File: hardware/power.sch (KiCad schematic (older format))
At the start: 18 parts, among them SW1 PM_BTN, U2 TPS63031DSKR, U5 BQ24075RGTT, U6 MAX16054AZT+T

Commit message: Removed 72 LEDs
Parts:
- BT1: symbol Battery -> Battery-RESCUE-blupoi
- L2: footprint Capacitors_SMD:C_0603 -> Resistors_SMD:R_1206
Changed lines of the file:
@@
 LIBS:micro_b_usb
 LIBS:blupoi-cache
-EELAYER 25 0
+EELAYER 26 0
 EELAYER END
 $Descr A4 11693 8268
@@
 F 0 "L2" H 4950 1865 50  0000 C CNN
 F 1 "1.5uH" H 4950 1774 50  0000 C CNN
-F 2 "Capacitors_SMD:C_0603" H 4950 1650 50  0001 C CNN
+F 2 "Resistors_SMD:R_1206" H 4950 1650 50  0001 C CNN
 F 3 "" H 4950 1650 50  0000 C CNN
 	1    4950 1650
@@
 $EndComp
 $Comp
-L Battery BT1
+L Battery-RESCUE-blupoi BT1
 U 1 1 579AD18C
 P 1850 2150
+AR Path="/579AD18C" Ref="BT1"  Part="1"
+AR Path="/57B9A02C/579AD18C" Ref="BT1"  Part="1"
 F 0 "BT1" V 1595 2150 50  0000 C CNN
 F 1 "Battery" V 1686 2150 50  0000 C CNN

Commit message: Power, add pulldown to bq24075 EN1
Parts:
- added R?: 10k, symbol R_Small
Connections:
- wire segments 81 -> 83
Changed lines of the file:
@@
 $Descr A4 11693 8268
 encoding utf-8
-Sheet 7 6
+Sheet 6 6
 Title ""
 Date ""
@@
 Text HLabel 6250 4750 2    60   Input ~ 0
 PM_EN2
-Text HLabel 5050 4850 2    60   Input ~ 0
+Text HLabel 6250 4850 2    60   Input ~ 0
 PM_EN1
 Text HLabel 5050 5050 2    60   Output ~ 0
@@
 	6050 4650 6050 4750
 Wire Wire Line
-	5050 4850 4950 4850
+	4950 4850 6250 4850
 Wire Wire Line
 	5250 5350 4950 5350
@@
 Text GLabel 3650 6850 0    60   Input ~ 0
 VBAT
+$Comp
+L R_Small R?
+U 1 1 5897F73B
+P 6050 5050
+F 0 "R?" H 6100 5150 50  0000 L CNN
+F 1 "10k" H 6100 4950 50  0000 L CNN
+F 2 "" H -100 100 50  0001 C CNN
+F 3 "" H -100 100 50  0001 C CNN
+	1    6050 5050
+	1    0    0    -1
+$EndComp
+Wire Wire Line
+	6050 4950 6050 4850
+Connection ~ 6050 4850
+$Comp
+L GND #PWR?
+U 1 1 5897F92D
+P 6050 5300
+F 0 "#PWR?" H 6100 5350 50  0001 C CNN
+F 1 "GND" H 6055 5127 50  0000 C CNN
+F 2 "" H -50 0   50  0001 C CNN
+F 3 "" H -50 0   50  0001 C CNN
+	1    6050 5300
+	1    0    0    -1
+$EndComp
+Wire Wire Line
+	6050 5300 6050 5150
 $EndSCHEMATC

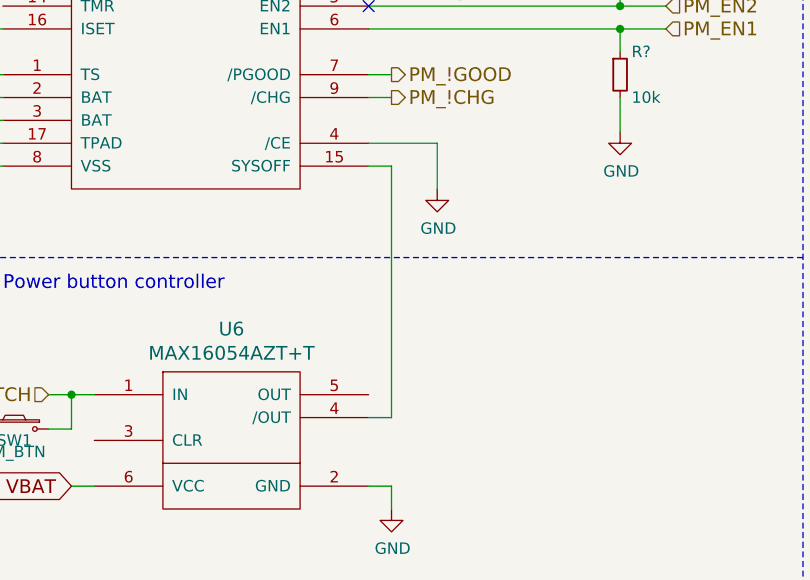
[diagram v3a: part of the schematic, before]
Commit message: Power, add pulldown to bq24075 SYSOFF
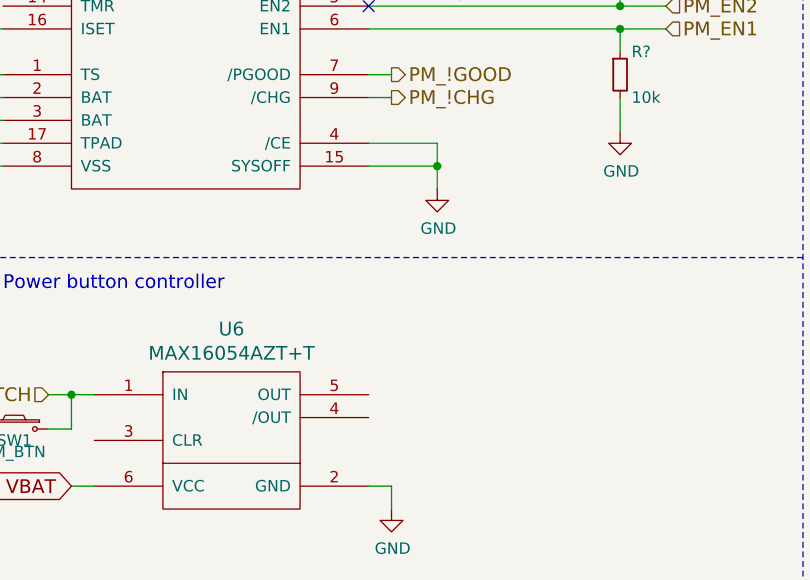
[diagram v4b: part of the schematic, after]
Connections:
- wire segments 83 -> 81
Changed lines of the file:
@@
 	3150 6600 3250 6600
 Wire Wire Line
-	4950 5450 5050 5450
-Wire Wire Line
-	5050 5450 5050 6550
-Wire Wire Line
-	5050 6550 4950 6550
+	4950 5450 5250 5450
 Wire Wire Line
 	3250 4450 3250 4300
@@
 Wire Wire Line
 	6050 5300 6050 5150
+Connection ~ 5250 5450
 $EndSCHEMATC

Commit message: Added sip32408 ic
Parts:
- added U7: sip32408, symbol sip32408
- R7: renamed from R?; footprint (none) -> Resistors_SMD:R_0603
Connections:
- net labels added: VCHG
- wire segments 81 -> 87
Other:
- moved on the sheet: SW1, U6
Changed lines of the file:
@@
 LIBS:max16054
 LIBS:micro_b_usb
+LIBS:sip32408
 LIBS:blupoi-cache
 EELAYER 26 0
@@
 $EndComp
 $Comp
-L GND #PWR017
+L GND #PWR23
 U 1 1 5794CAF3
 P 4200 2650
-F 0 "#PWR017" H 4200 2400 50  0001 C CNN
+F 0 "#PWR23" H 4200 2400 50  0001 C CNN
 F 1 "GND" H 4205 2477 50  0000 C CNN
 F 2 "" H 4200 2650 50  0000 C CNN
@@
 $EndComp
 $Comp
-L GND #PWR018
+L GND #PWR26
 U 1 1 5794CB19
 P 5750 2650
-F 0 "#PWR018" H 5750 2400 50  0001 C CNN
+F 0 "#PWR26" H 5750 2400 50  0001 C CNN
 F 1 "GND" H 5755 2477 50  0000 C CNN
 F 2 "" H 5750 2650 50  0000 C CNN
@@
 $EndComp
 $Comp
-L GND #PWR019
+L GND #PWR27
 U 1 1 5794D124
 P 5900 2550
-F 0 "#PWR019" H 5900 2300 50  0001 C CNN
+F 0 "#PWR27" H 5900 2300 50  0001 C CNN
 F 1 "GND" H 5905 2377 50  0000 C CNN
 F 2 "" H 5900 2550 50  0000 C CNN
@@
 $EndComp
 $Comp
-L GND #PWR020
+L GND #PWR29
 U 1 1 5794D140
 P 6200 2550
-F 0 "#PWR020" H 6200 2300 50  0001 C CNN
+F 0 "#PWR29" H 6200 2300 50  0001 C CNN
 F 1 "GND" H 6205 2377 50  0000 C CNN
 F 2 "" H 6200 2550 50  0000 C CNN
@@
 $EndComp
 $Comp
-L GND #PWR021
+L GND #PWR21
 U 1 1 5794D3C8
 P 3650 2550
-F 0 "#PWR021" H 3650 2300 50  0001 C CNN
+F 0 "#PWR21" H 3650 2300 50  0001 C CNN
 F 1 "GND" H 3655 2377 50  0000 C CNN
 F 2 "" H 3650 2550 50  0000 C CNN
@@
 $EndComp
 $Comp
-L GND #PWR022
+L GND #PWR17
 U 1 1 579AD335
 P 1600 2250
-F 0 "#PWR022" H 1600 2000 50  0001 C CNN
+F 0 "#PWR17" H 1600 2000 50  0001 C CNN
 F 1 "GND" H 1605 2077 50  0000 C CNN
 F 2 "" H 1600 2250 50  0000 C CNN
@@
 VUSB
 $Comp
-L GND #PWR023
+L GND #PWR20
 U 1 1 57B8A1CB
 P 3250 5550
-F 0 "#PWR023" H 3250 5300 50  0001 C CNN
+F 0 "#PWR20" H 3250 5300 50  0001 C CNN
 F 1 "GND" H 3255 5377 50  0000 C CNN
 F 2 "" H 3250 5550 50  0000 C CNN
@@
 PM_!CHG
 $Comp
-L GND #PWR024
+L GND #PWR24
 U 1 1 57B8B68E
 P 5250 5550
-F 0 "#PWR024" H 5250 5300 50  0001 C CNN
+F 0 "#PWR24" H 5250 5300 50  0001 C CNN
 F 1 "GND" H 5255 5377 50  0000 C CNN
 F 2 "" H 5250 5550 50  0000 C CNN
@@
 	1    0    0    -1
 $EndComp
-Text HLabel 5650 4050 2    60   Output ~ 0
+Text HLabel 5300 6400 2    60   Output ~ 0
 VIN
 $Comp
 L MAX16054 U6
 U 1 1 57B90098
-P 4350 6650
-F 0 "U6" H 4350 7137 60  0000 C CNN
-F 1 "MAX16054AZT+T" H 4350 7031 60  0000 C CNN
-F 2 "tinkerforge-libraries:SOT23-6" H 4350 6650 60  0001 C CNN
-F 3 "" H 4350 6650 60  0001 C CNN
-	1    4350 6650
-	1    0    0    -1
-$EndComp
-$Comp
-L GND #PWR025
+P 3100 6750
+F 0 "U6" H 3100 7237 60  0000 C CNN
+F 1 "MAX16054AZT+T" H 3100 7131 60  0000 C CNN
+F 2 "tinkerforge-libraries:SOT23-6" H 3100 6750 60  0001 C CNN
+F 3 "" H 3100 6750 60  0001 C CNN
+	1    3100 6750
+	1    0    0    -1
+$EndComp
+$Comp
+L GND #PWR22
 U 1 1 57B90631
-P 5050 6950
-F 0 "#PWR025" H 5050 6700 50  0001 C CNN
-F 1 "GND" H 5055 6777 50  0000 C CNN
-F 2 "" H 5050 6950 50  0000 C CNN
-F 3 "" H 5050 6950 50  0000 C CNN
-	1    5050 6950
-	1    0    0    -1
-$EndComp
-Text HLabel 3550 6450 0    60   Input ~ 0
+P 3800 7050
+F 0 "#PWR22" H 3800 6800 50  0001 C CNN
+F 1 "GND" H 3805 6877 50  0000 C CNN
+F 2 "" H 3800 7050 50  0000 C CNN
+F 3 "" H 3800 7050 50  0000 C CNN
+	1    3800 7050
+	1    0    0    -1
+$EndComp
+Text HLabel 2300 6550 0    60   Input ~ 0
 PM_SWITCH
 $Comp
 L SW_PUSH_SMALL_H SW1
 U 1 1 57B90C56
-P 3400 6600
-F 0 "SW1" H 3400 6550 50  0000 C CNN
-F 1 "PM_BTN" H 3400 6500 50  0000 C CNN
-F 2 "footprints:switch_spst_smd_5.5mm_4.5mm" H 3400 6800 50  0001 C CNN
-F 3 "" H 3400 6800 50  0000 C CNN
-	1    3400 6600
-	1    0    0    -1
-$EndComp
-$Comp
-L GND #PWR026
+P 2150 6700
+F 0 "SW1" H 2150 6650 50  0000 C CNN
+F 1 "PM_BTN" H 2150 6600 50  0000 C CNN
+F 2 "footprints:switch_spst_smd_5.5mm_4.5mm" H 2150 6900 50  0001 C CNN
+F 3 "" H 2150 6900 50  0000 C CNN
+	1    2150 6700
+	1    0    0    -1
+$EndComp
+$Comp
+L GND #PWR18
 U 1 1 57B911A1
-P 3150 6700
-F 0 "#PWR026" H 3150 6450 50  0001 C CNN
-F 1 "GND" H 3155 6527 50  0000 C CNN
-F 2 "" H 3150 6700 50  0000 C CNN
-F 3 "" H 3150 6700 50  0000 C CNN
-	1    3150 6700
+P 1900 6800
+F 0 "#PWR18" H 1900 6550 50  0001 C CNN
+F 1 "GND" H 1905 6627 50  0000 C CNN
+F 2 "" H 1900 6800 50  0000 C CNN
+F 3 "" H 1900 6800 50  0000 C CNN
+	1    1900 6800
 	1    0    0    -1
 $EndComp
@@
 $EndComp
 $Comp
-L GND #PWR027
+L GND #PWR19
 U 1 1 57B91E3C
 P 2850 4450
-F 0 "#PWR027" H 2850 4200 50  0001 C CNN
+F 0 "#PWR19" H 2850 4200 50  0001 C CNN
 F 1 "GND" V 2855 4322 50  0000 R CNN
 F 2 "" H 2850 4450 50  0000 C CNN
@@
 Connection ~ 5050 4450
 Wire Wire Line
-	5050 6950 5050 6850
-Wire Wire Line
-	5050 6850 4950 6850
-Wire Wire Line
-	3750 6850 3650 6850
-Wire Wire Line
-	3550 6450 3750 6450
-Wire Wire Line
-	3650 6450 3650 6600
-Wire Wire Line
-	3650 6600 3550 6600
-Connection ~ 3650 6450
-Wire Wire Line
-	3150 6700 3150 6600
-Wire Wire Line
-	3150 6600 3250 6600
+	3800 7050 3800 6950
+Wire Wire Line
+	3800 6950 3700 6950
+Wire Wire Line
+	2500 6950 2400 6950
+Wire Wire Line
+	2300 6550 2500 6550
+Wire Wire Line
+	2400 6550 2400 6700
+Wire Wire Line
+	2400 6700 2300 6700
+Connection ~ 2400 6550
+Wire Wire Line
+	1900 6800 1900 6700
+Wire Wire Line
+	1900 6700 2000 6700
 Wire Wire Line
 	4950 5450 5250 5450
@@
 	5050 4050 5050 4550
 $Comp
-L GND #PWR028
+L GND #PWR25
 U 1 1 57BA2103
 P 5400 4550
-F 0 "#PWR028" H 5400 4300 50  0001 C CNN
+F 0 "#PWR25" H 5400 4300 50  0001 C CNN
 F 1 "GND" H 5400 4400 50  0000 C CNN
 F 2 "" H 5400 4550 50  0000 C CNN
@@
 Wire Wire Line
 	5400 4550 5400 4450
-Text GLabel 3650 6850 0    60   Input ~ 0
+Text GLabel 2400 6950 0    60   Input ~ 0
 VBAT
 $Comp
-L R_Small R?
+L R_Small R7
 U 1 1 5897F73B
 P 6050 5050
-F 0 "R?" H 6100 5150 50  0000 L CNN
+F 0 "R7" H 6100 5150 50  0000 L CNN
 F 1 "10k" H 6100 4950 50  0000 L CNN
-F 2 "" H -100 100 50  0001 C CNN
+F 2 "Resistors_SMD:R_0603" H -100 100 50  0001 C CNN
 F 3 "" H -100 100 50  0001 C CNN
 	1    6050 5050
@@
 Connection ~ 6050 4850
 $Comp
-L GND #PWR?
+L GND #PWR28
 U 1 1 5897F92D
 P 6050 5300
-F 0 "#PWR?" H 6100 5350 50  0001 C CNN
+F 0 "#PWR28" H 6100 5350 50  0001 C CNN
 F 1 "GND" H 6055 5127 50  0000 C CNN
 F 2 "" H -50 0   50  0001 C CNN
@@
 	6050 5300 6050 5150
 Connection ~ 5250 5450
+$Comp
+L sip32408 U7
+U 1 1 58980243
+P 4850 6300
+F 0 "U7" H 4875 6487 60  0000 C CNN
+F 1 "sip32408" H 4875 6381 60  0000 C CNN
+F 2 "" H -3550 1850 60  0001 C CNN
+F 3 "" H -3550 1850 60  0001 C CNN
+	1    4850 6300
+	1    0    0    -1
+$EndComp
+Wire Wire Line
+	4600 6400 4500 6400
+Wire Wire Line
+	4600 6550 3700 6550
+Wire Wire Line
+	5150 6550 5250 6550
+Wire Wire Line
+	5250 6550 5250 6700
+Wire Wire Line
+	5250 6700 5150 6700
+Wire Wire Line
+	5300 6400 5150 6400
+Text GLabel 5650 4050 2    60   Input ~ 0
+VCHG
+Text GLabel 4500 6400 0    60   Input ~ 0
+VCHG
 $EndSCHEMATC

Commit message: Switched to fat small design
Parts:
- removed BT1: Battery, 16650_holder:16650_in_pcb_socket, symbol Battery-RESCUE-blupoi
- added BT1: Battery_Cell, 16650_holder:16650_in_pcb_socket, symbol Battery_Cell
- U7: footprint (none) -> sip32408:sip32408
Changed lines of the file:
@@
 $EndComp
 $Comp
-L GND #PWR23
+L GND #PWR015
 U 1 1 5794CAF3
 P 4200 2650
-F 0 "#PWR23" H 4200 2400 50  0001 C CNN
+F 0 "#PWR015" H 4200 2400 50  0001 C CNN
 F 1 "GND" H 4205 2477 50  0000 C CNN
 F 2 "" H 4200 2650 50  0000 C CNN
@@
 $EndComp
 $Comp
-L GND #PWR26
+L GND #PWR016
 U 1 1 5794CB19
 P 5750 2650
-F 0 "#PWR26" H 5750 2400 50  0001 C CNN
+F 0 "#PWR016" H 5750 2400 50  0001 C CNN
 F 1 "GND" H 5755 2477 50  0000 C CNN
 F 2 "" H 5750 2650 50  0000 C CNN
@@
 $EndComp
 $Comp
-L GND #PWR27
+L GND #PWR017
 U 1 1 5794D124
 P 5900 2550
-F 0 "#PWR27" H 5900 2300 50  0001 C CNN
+F 0 "#PWR017" H 5900 2300 50  0001 C CNN
 F 1 "GND" H 5905 2377 50  0000 C CNN
 F 2 "" H 5900 2550 50  0000 C CNN
@@
 $EndComp
 $Comp
-L GND #PWR29
+L GND #PWR018
 U 1 1 5794D140
 P 6200 2550
-F 0 "#PWR29" H 6200 2300 50  0001 C CNN
+F 0 "#PWR018" H 6200 2300 50  0001 C CNN
 F 1 "GND" H 6205 2377 50  0000 C CNN
 F 2 "" H 6200 2550 50  0000 C CNN
@@
 $EndComp
 $Comp
-L GND #PWR21
+L GND #PWR019
 U 1 1 5794D3C8
 P 3650 2550
-F 0 "#PWR21" H 3650 2300 50  0001 C CNN
+F 0 "#PWR019" H 3650 2300 50  0001 C CNN
 F 1 "GND" H 3655 2377 50  0000 C CNN
 F 2 "" H 3650 2550 50  0000 C CNN
@@
 $EndComp
 $Comp
-L Battery-RESCUE-blupoi BT1
-U 1 1 579AD18C
-P 1850 2150
-AR Path="/579AD18C" Ref="BT1"  Part="1"
-AR Path="/57B9A02C/579AD18C" Ref="BT1"  Part="1"
-F 0 "BT1" V 1595 2150 50  0000 C CNN
-F 1 "Battery" V 1686 2150 50  0000 C CNN
-F 2 "16650_holder:16650_in_pcb_socket" V 1850 2190 50  0001 C CNN
-F 3 "" V 1850 2190 50  0000 C CNN
-	1    1850 2150
-	0    1    1    0
-$EndComp
-$Comp
-L GND #PWR17
+L GND #PWR020
 U 1 1 579AD335
 P 1600 2250
-F 0 "#PWR17" H 1600 2000 50  0001 C CNN
+F 0 "#PWR020" H 1600 2000 50  0001 C CNN
 F 1 "GND" H 1605 2077 50  0000 C CNN
 F 2 "" H 1600 2250 50  0000 C CNN
@@
 VUSB
 $Comp
-L GND #PWR20
+L GND #PWR021
 U 1 1 57B8A1CB
 P 3250 5550
-F 0 "#PWR20" H 3250 5300 50  0001 C CNN
+F 0 "#PWR021" H 3250 5300 50  0001 C CNN
 F 1 "GND" H 3255 5377 50  0000 C CNN
 F 2 "" H 3250 5550 50  0000 C CNN
@@
 PM_!CHG
 $Comp
-L GND #PWR24
+L GND #PWR022
 U 1 1 57B8B68E
 P 5250 5550
-F 0 "#PWR24" H 5250 5300 50  0001 C CNN
+F 0 "#PWR022" H 5250 5300 50  0001 C CNN
 F 1 "GND" H 5255 5377 50  0000 C CNN
 F 2 "" H 5250 5550 50  0000 C CNN
@@
 $EndComp
 $Comp
-L GND #PWR22
+L GND #PWR023
 U 1 1 57B90631
 P 3800 7050
-F 0 "#PWR22" H 3800 6800 50  0001 C CNN
+F 0 "#PWR023" H 3800 6800 50  0001 C CNN
 F 1 "GND" H 3805 6877 50  0000 C CNN
 F 2 "" H 3800 7050 50  0000 C CNN
@@
 $EndComp
 $Comp
-L GND #PWR18
+L GND #PWR024
 U 1 1 57B911A1
 P 1900 6800
-F 0 "#PWR18" H 1900 6550 50  0001 C CNN
+F 0 "#PWR024" H 1900 6550 50  0001 C CNN
 F 1 "GND" H 1905 6627 50  0000 C CNN
 F 2 "" H 1900 6800 50  0000 C CNN
@@
 $EndComp
 $Comp
-L GND #PWR19
+L GND #PWR025
 U 1 1 57B91E3C
 P 2850 4450
-F 0 "#PWR19" H 2850 4200 50  0001 C CNN
+F 0 "#PWR025" H 2850 4200 50  0001 C CNN
 F 1 "GND" V 2855 4322 50  0000 R CNN
 F 2 "" H 2850 4450 50  0000 C CNN
@@
 	5050 4050 5050 4550
 $Comp
-L GND #PWR25
+L GND #PWR026
 U 1 1 57BA2103
 P 5400 4550
-F 0 "#PWR25" H 5400 4300 50  0001 C CNN
+F 0 "#PWR026" H 5400 4300 50  0001 C CNN
 F 1 "GND" H 5400 4400 50  0000 C CNN
 F 2 "" H 5400 4550 50  0000 C CNN
@@
 Connection ~ 6050 4850
 $Comp
-L GND #PWR28
+L GND #PWR027
 U 1 1 5897F92D
 P 6050 5300
-F 0 "#PWR28" H 6100 5350 50  0001 C CNN
+F 0 "#PWR027" H 6100 5350 50  0001 C CNN
 F 1 "GND" H 6055 5127 50  0000 C CNN
 F 2 "" H -50 0   50  0001 C CNN
@@
 F 0 "U7" H 4875 6487 60  0000 C CNN
 F 1 "sip32408" H 4875 6381 60  0000 C CNN
-F 2 "" H -3550 1850 60  0001 C CNN
+F 2 "sip32408:sip32408" H -3550 1850 60  0001 C CNN
 F 3 "" H -3550 1850 60  0001 C CNN
 	1    4850 6300
@@
 Text GLabel 4500 6400 0    60   Input ~ 0
 VCHG
+$Comp
+L Battery_Cell BT1
+U 1 1 58A28802
+P 1800 2150
+F 0 "BT1" V 1545 2200 50  0000 C CNN
+F 1 "Battery_Cell" V 1636 2200 50  0000 C CNN
+F 2 "16650_holder:16650_in_pcb_socket" V 150 210 50  0001 C CNN
+F 3 "" V 150 210 50  0001 C CNN
+	1    1800 2150
+	0    1    1    0
+$EndComp
 $EndSCHEMATC

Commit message: Fixed broken inductor schematic
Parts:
- L2: symbol INDUCTOR_SMALL -> L_Small
- SW1: footprint footprints:switch_spst_smd_5.5mm_4.5mm -> kss241glfs:KSS241GLFS; symbol SW_PUSH_SMALL_H -> SW_SPST
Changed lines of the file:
@@
 LIBS:micro_b_usb
 LIBS:sip32408
+LIBS:switches
 LIBS:blupoi-cache
 EELAYER 26 0
@@
 $EndDescr
 $Comp
-L INDUCTOR_SMALL L2
+L L_Small L2
 U 1 1 57952421
 P 4950 1650
-F 0 "L2" H 4950 1865 50  0000 C CNN
-F 1 "1.5uH" H 4950 1774 50  0000 C CNN
+F 0 "L2" V 5150 1650 50  0000 C CNN
+F 1 "1.5uH" V 5050 1650 50  0000 C CNN
 F 2 "Resistors_SMD:R_1206" H 4950 1650 50  0001 C CNN
 F 3 "" H 4950 1650 50  0000 C CNN
 	1    4950 1650
-	1    0    0    -1
+	0    -1   -1   0
 $EndComp
 $Comp
@@
 $EndComp
 $Comp
-L GND #PWR015
+L GND #PWR016
 U 1 1 5794CAF3
 P 4200 2650
-F 0 "#PWR015" H 4200 2400 50  0001 C CNN
+F 0 "#PWR016" H 4200 2400 50  0001 C CNN
 F 1 "GND" H 4205 2477 50  0000 C CNN
 F 2 "" H 4200 2650 50  0000 C CNN
@@
 $EndComp
 $Comp
-L GND #PWR016
+L GND #PWR017
 U 1 1 5794CB19
 P 5750 2650
-F 0 "#PWR016" H 5750 2400 50  0001 C CNN
+F 0 "#PWR017" H 5750 2400 50  0001 C CNN
 F 1 "GND" H 5755 2477 50  0000 C CNN
 F 2 "" H 5750 2650 50  0000 C CNN
@@
 $EndComp
 $Comp
-L GND #PWR017
+L GND #PWR018
 U 1 1 5794D124
 P 5900 2550
-F 0 "#PWR017" H 5900 2300 50  0001 C CNN
+F 0 "#PWR018" H 5900 2300 50  0001 C CNN
 F 1 "GND" H 5905 2377 50  0000 C CNN
 F 2 "" H 5900 2550 50  0000 C CNN
@@
 $EndComp
 $Comp
-L GND #PWR018
+L GND #PWR019
 U 1 1 5794D140
 P 6200 2550
-F 0 "#PWR018" H 6200 2300 50  0001 C CNN
+F 0 "#PWR019" H 6200 2300 50  0001 C CNN
 F 1 "GND" H 6205 2377 50  0000 C CNN
 F 2 "" H 6200 2550 50  0000 C CNN
@@
 $EndComp
 $Comp
-L GND #PWR019
+L GND #PWR020
 U 1 1 5794D3C8
 P 3650 2550
-F 0 "#PWR019" H 3650 2300 50  0001 C CNN
+F 0 "#PWR020" H 3650 2300 50  0001 C CNN
 F 1 "GND" H 3655 2377 50  0000 C CNN
 F 2 "" H 3650 2550 50  0000 C CNN
@@
 $EndComp
 $Comp
-L GND #PWR020
+L GND #PWR021
 U 1 1 579AD335
 P 1600 2250
-F 0 "#PWR020" H 1600 2000 50  0001 C CNN
+F 0 "#PWR021" H 1600 2000 50  0001 C CNN
 F 1 "GND" H 1605 2077 50  0000 C CNN
 F 2 "" H 1600 2250 50  0000 C CNN
@@
 VUSB
 $Comp
-L GND #PWR021
+L GND #PWR022
 U 1 1 57B8A1CB
 P 3250 5550
-F 0 "#PWR021" H 3250 5300 50  0001 C CNN
+F 0 "#PWR022" H 3250 5300 50  0001 C CNN
 F 1 "GND" H 3255 5377 50  0000 C CNN
 F 2 "" H 3250 5550 50  0000 C CNN
@@
 PM_!CHG
 $Comp
-L GND #PWR022
+L GND #PWR023
 U 1 1 57B8B68E
 P 5250 5550
-F 0 "#PWR022" H 5250 5300 50  0001 C CNN
+F 0 "#PWR023" H 5250 5300 50  0001 C CNN
 F 1 "GND" H 5255 5377 50  0000 C CNN
 F 2 "" H 5250 5550 50  0000 C CNN
@@
 $EndComp
 $Comp
-L GND #PWR023
+L GND #PWR024
 U 1 1 57B90631
 P 3800 7050
-F 0 "#PWR023" H 3800 6800 50  0001 C CNN
+F 0 "#PWR024" H 3800 6800 50  0001 C CNN
 F 1 "GND" H 3805 6877 50  0000 C CNN
 F 2 "" H 3800 7050 50  0000 C CNN
@@
 PM_SWITCH
 $Comp
-L SW_PUSH_SMALL_H SW1
-U 1 1 57B90C56
-P 2150 6700
-F 0 "SW1" H 2150 6650 50  0000 C CNN
-F 1 "PM_BTN" H 2150 6600 50  0000 C CNN
-F 2 "footprints:switch_spst_smd_5.5mm_4.5mm" H 2150 6900 50  0001 C CNN
-F 3 "" H 2150 6900 50  0000 C CNN
-	1    2150 6700
-	1    0    0    -1
-$EndComp
-$Comp
-L GND #PWR024
+L GND #PWR025
 U 1 1 57B911A1
-P 1900 6800
-F 0 "#PWR024" H 1900 6550 50  0001 C CNN
-F 1 "GND" H 1905 6627 50  0000 C CNN
-F 2 "" H 1900 6800 50  0000 C CNN
-F 3 "" H 1900 6800 50  0000 C CNN
-	1    1900 6800
+P 1800 6850
+F 0 "#PWR025" H 1800 6600 50  0001 C CNN
+F 1 "GND" H 1805 6677 50  0000 C CNN
+F 2 "" H 1800 6850 50  0000 C CNN
+F 3 "" H 1800 6850 50  0000 C CNN
+	1    1800 6850
 	1    0    0    -1
 $EndComp
@@
 $EndComp
 $Comp
-L GND #PWR025
+L GND #PWR026
 U 1 1 57B91E3C
 P 2850 4450
-F 0 "#PWR025" H 2850 4200 50  0001 C CNN
+F 0 "#PWR026" H 2850 4200 50  0001 C CNN
 F 1 "GND" V 2855 4322 50  0000 R CNN
 F 2 "" H 2850 4450 50  0000 C CNN
@@
 	3650 2150 4300 2150
 Wire Wire Line
-	4700 1650 4200 1650
-Wire Wire Line
-	5200 1650 5750 1650
+	4200 1650 4850 1650
+Wire Wire Line
+	5050 1650 5750 1650
 Wire Wire Line
 	2100 2050 2100 2150
@@
 	2300 6550 2500 6550
 Wire Wire Line
-	2400 6550 2400 6700
-Wire Wire Line
-	2400 6700 2300 6700
+	2400 6550 2400 6750
 Connection ~ 2400 6550
-Wire Wire Line
-	1900 6800 1900 6700
-Wire Wire Line
-	1900 6700 2000 6700
 Wire Wire Line
 	4950 5450 5250 5450
@@
 	5050 4050 5050 4550
 $Comp
-L GND #PWR026
+L GND #PWR027
 U 1 1 57BA2103
 P 5400 4550
-F 0 "#PWR026" H 5400 4300 50  0001 C CNN
+F 0 "#PWR027" H 5400 4300 50  0001 C CNN
 F 1 "GND" H 5400 4400 50  0000 C CNN
 F 2 "" H 5400 4550 50  0000 C CNN
@@
 Connection ~ 6050 4850
 $Comp
-L GND #PWR027
+L GND #PWR028
 U 1 1 5897F92D
 P 6050 5300
-F 0 "#PWR027" H 6100 5350 50  0001 C CNN
+F 0 "#PWR028" H 6100 5350 50  0001 C CNN
 F 1 "GND" H 6055 5127 50  0000 C CNN
 F 2 "" H -50 0   50  0001 C CNN
@@
 	0    1    1    0
 $EndComp
+$Comp
+L SW_SPST SW1
+U 1 1 57B90C56
+P 2100 6750
+F 0 "SW1" H 2100 6800 50  0000 C CNN
+F 1 "PM_BTN" H 2100 6700 50  0000 C CNN
+F 2 "kss241glfs:KSS241GLFS" H 2100 6950 50  0001 C CNN
+F 3 "" H 2100 6950 50  0000 C CNN
+	1    2100 6750
+	1    0    0    -1
+$EndComp
+Wire Wire Line
+	2300 6750 2500 6750
+Connection ~ 2400 6750
+Wire Wire Line
+	1900 6750 1800 6750
+Wire Wire Line
+	1800 6750 1800 6850
 $EndSCHEMATC

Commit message: Change net name from VCHG to VREG
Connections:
- net labels added: VREG
- net labels removed: VCHG
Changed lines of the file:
@@
 	5300 6400 5150 6400
 Text GLabel 5650 4050 2    60   Input ~ 0
-VCHG
+VREG
 Text GLabel 4500 6400 0    60   Input ~ 0
-VCHG
+VREG
 $Comp
 L Battery_Cell BT1
